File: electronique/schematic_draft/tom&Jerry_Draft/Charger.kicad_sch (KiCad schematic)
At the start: 56 parts, among them J201 Conn_01x02, J201 USB_C_Receptacle_USB2.0_16P, J202 Conn_01x02, J203 Conn_01x02, Q201 PMOS, U201 MP1475DJ-LF-P, U202 BQ25172DSGR

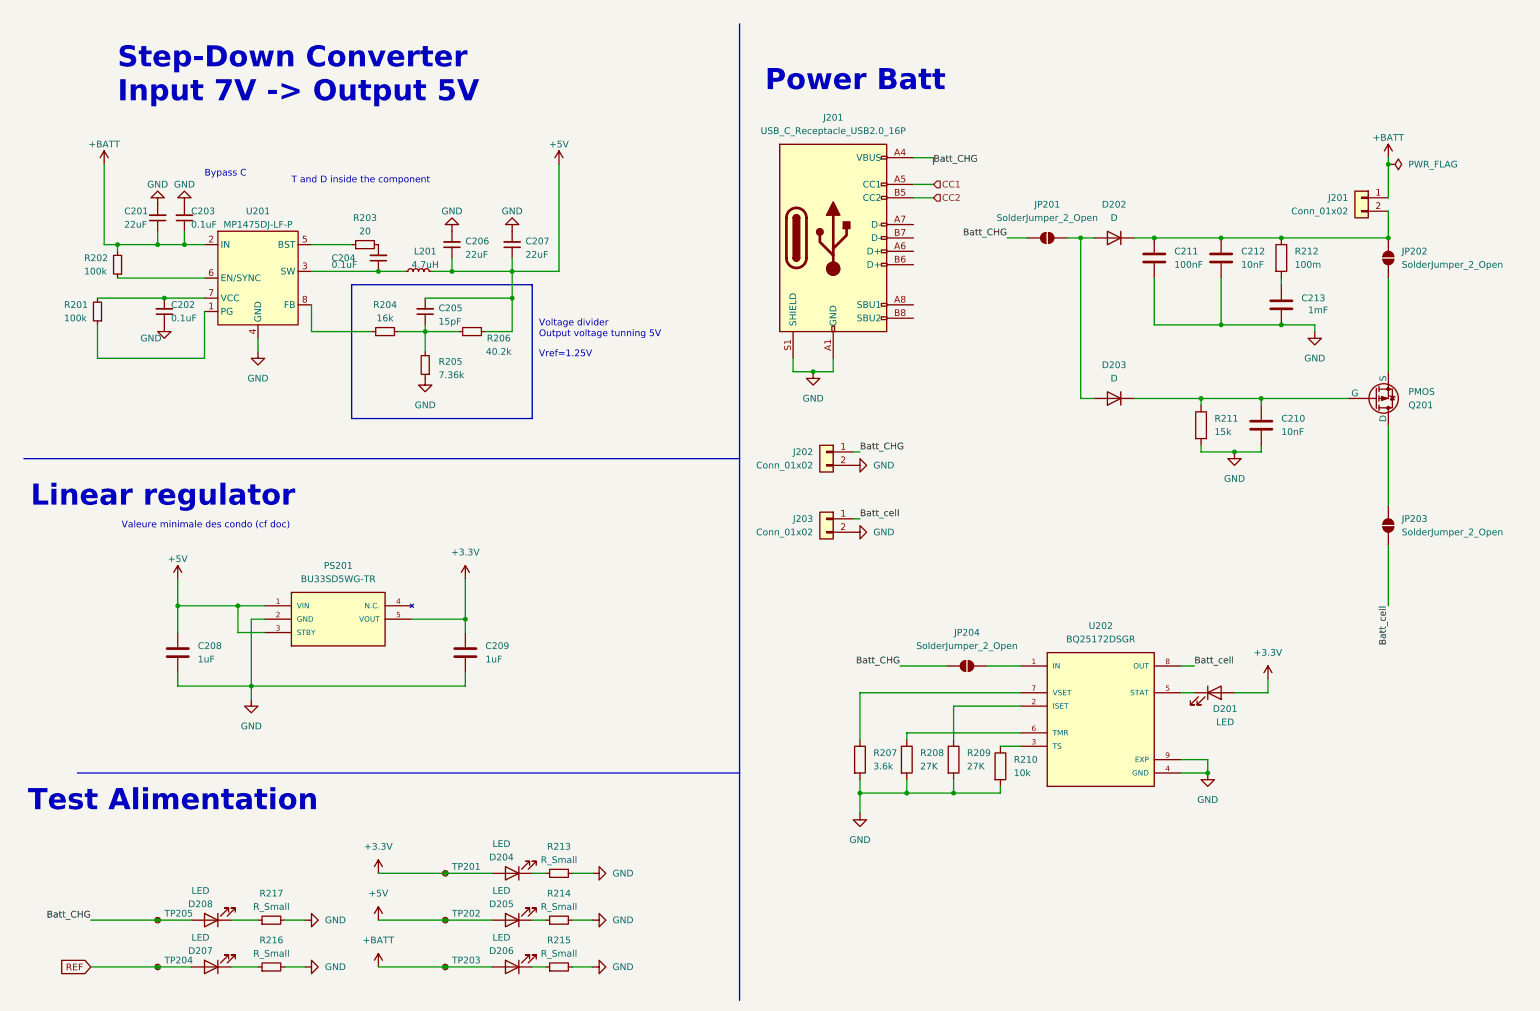
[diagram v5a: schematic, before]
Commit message: STM32 KiCAD v2.0 x CubeIDE - Pin definitif + schematic reviewed
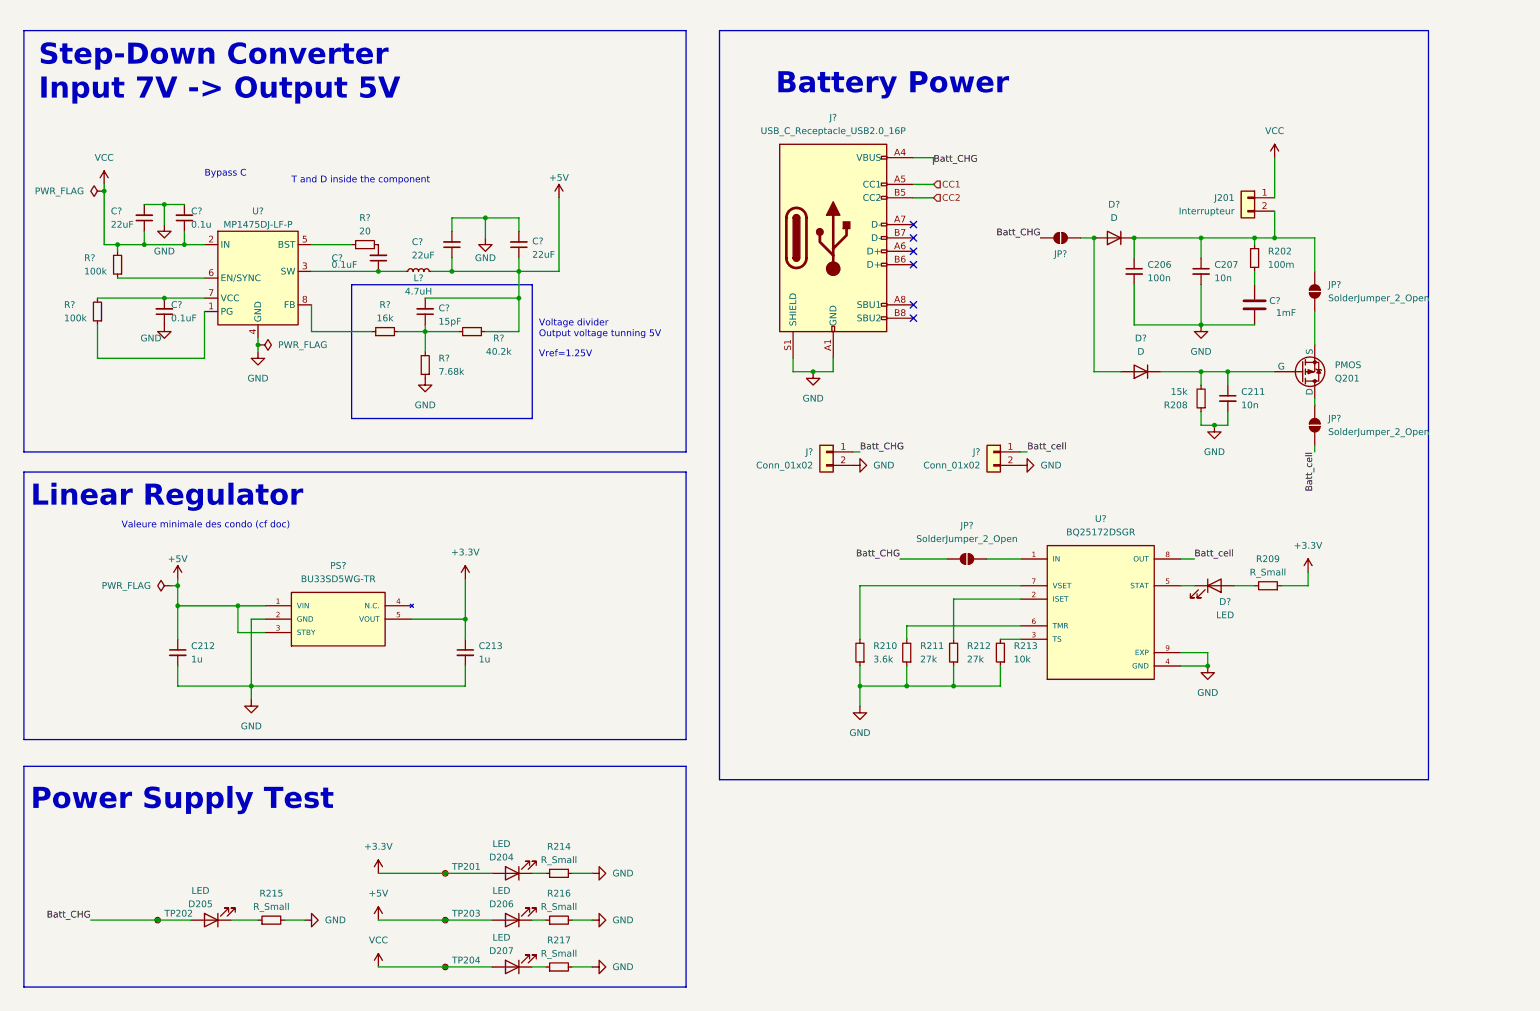
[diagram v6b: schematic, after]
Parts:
- removed C208, C209: 1uF, symbol Device:C
- removed C210, C212: 10nF, symbol Device:C
- removed C211: 100nF, symbol Device:C
- removed D207: LED, symbol Device:LED
- removed R207: 3.6k, symbol Device:R
- removed R208, R209: 27K, symbol Device:R
- removed R210: 10k, symbol Device:R
- removed R211: 15k, symbol Device:R
- removed R212: 100m, symbol Device:R
- removed R216: R_Small, symbol Device:R_Small
- removed TP204: TestPoint_Small, symbol Connector:TestPoint_Small
- added C206: 100n, symbol Device:C_Small
- added C207, C211: 10n, symbol Device:C_Small
- added C212, C213: 1u, symbol Device:C_Small
- added R202: 100m, symbol Device:R_Small
- added R208: 15k, symbol Device:R_Small
- added R209: R_Small, symbol Device:R_Small
- added R210: 3.6k, symbol Device:R_Small
- added R211, R212: 27k, symbol Device:R_Small
- added R213: 10k, symbol Device:R_Small
- C?: renamed from C203; value 0.1uF -> 0.1u
- J201: value Conn_01x02 -> Interrupteur
- R?: renamed from R205; value 7.36k -> 7.68k
- renumbered C213 to C?, C201 to C?, C202 to C?, C207 to C?, C206 to C?, C204 to C?, C205 to C?, D208 to D205, D205 to D206, D206 to D207, D203 to D?, D202 to D?, D201 to D?, J202 to J?, J203 to J?, J201 to J?, JP202 to JP?, JP204 to JP?, JP201 to JP?, JP203 to JP?, L201 to L?, PS201 to PS?, R213 to R214, R217 to R215, R214 to R216, R215 to R217, R206 to R?, R201 to R?, R204 to R?, R203 to R?, R202 to R?, TP205 to TP202, TP202 to TP203, TP203 to TP204, U202 to U?, U201 to U?
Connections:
- net +3.3V: now also C213.1, R209.1; no longer D?.2 (A)
- net +5V: now also L?.1, C212.1; no longer L?.2
- net GND: now also C206.2, C207.2, C211.2, C212.2, C213.2, R208.1, R210.1, R211.1, R212.1, R213.1
- net at D?.1 (K), Q201.2 (G): now also C211.1, R208.2
- net at C?.1: now also R202.2
- net at D?.1 (K), J201.2 (Pin_2), JP?.2 (B): now also C206.1, C207.1, R202.1
- net at C?.1, U?.3 (SW): now also L?.2; no longer L?.1
- net at U?.6 (TMR): now also R211.2
- net at U?.2 (ISET): now also R212.2
- net at U?.3 (TS): now also R213.2
- net at U?.7 (VSET): now also R210.2
- net +BATT renamed VCC
- new net: D?.2 (A), R209.2
- no-connect marks 0 -> 6
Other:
- note added: "Battery Power"
- note added: "Linear Regulator"
- note added: "Power Supply Test"
- note removed: "Linear regulator"
- note removed: "Power Batt"
- note removed: "Test Alimentation"
- moved on the sheet: C?, D?, J201, J?, JP?, L?, Q201, U?

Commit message: Adding footprint V0.1
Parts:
- C206, C207, C211: footprint (none) -> Capacitor_SMD:C_0402_1005Metric
- C212, C213: footprint (none) -> Capacitor_SMD:C_0603_1608Metric
- C? (x4): footprint Capacitor_SMD:C_0603_1608Metric_Pad1.08x0.95mm_HandSolder -> Capacitor_SMD:C_0402_1005Metric
- C?: footprint (none) -> Tom&Jerry:PQFN80P300X500X100-14N
- C? (x3): footprint Capacitor_SMD:C_0603_1608Metric_Pad1.08x0.95mm_HandSolder -> Capacitor_SMD:C_0805_2012Metric
- D204, D205, D206, D207, D?: footprint (none) -> LED_SMD:LED_0603_1608Metric_Pad1.05x0.95mm_HandSolder
- J201: footprint (none) -> Tom&Jerry:Switch-3
- J? (x2): footprint (none) -> Connector_JST:JST_XH_S2B-XH-A-1_1x02_P2.50mm_Horizontal
- J?: footprint (none) -> Connector_USB:USB_C_Receptacle_HRO_TYPE-C-31-M-12
- JP? (x4): footprint (none) -> Jumper:SolderJumper-2_P1.3mm_Open_TrianglePad1.0x1.5mm
- L?: footprint Library:INDPM4141X210N -> Inductor_SMD:L_0603_1608Metric_Pad1.05x0.95mm_HandSolder
- PS?: footprint BU33SD5WG-TR:SOT95P280X125-5N -> Tom&Jerry:SOT95P280X125-5N
- R202, R208, R209, R210, R211, R212, R213: footprint (none) -> Resistor_SMD:R_0402_1005Metric
- R214, R215, R216, R217: value R_Small -> 3.3k; footprint (none) -> Resistor_SMD:R_0402_1005Metric
- R? (x5): footprint Resistor_SMD:R_0603_1608Metric_Pad0.98x0.95mm_HandSolder -> Resistor_SMD:R_0402_1005Metric
- R?: footprint Resistor_SMD:R_0805_2012Metric_Pad1.20x1.40mm_HandSolder -> Resistor_SMD:R_0402_1005Metric
- TP201, TP202, TP203, TP204: footprint (none) -> Test_Point:TestPoint_Pad_D1.5mm
- U?: footprint BQ25172DSGR:IC_BQ25172DSGR -> Tom&Jerry:IC_BQ25172DSGR
- U?: footprint Library:SOT65P280X100-8N -> Tom&Jerry:SOT65P280X100-8N
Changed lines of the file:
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@@
 			)
 		)
-		(property "Footprint" "Capacitor_SMD:C_0603_1608Metric_Pad1.08x0.95mm_HandSolder"
+		(property "Footprint" "Capacitor_SMD:C_0402_1005Metric"
 			(at 45.72 50.8 0)
 			(effects
@@
 			)
 		)
-		(property "Footprint" ""
+		(property "Footprint" "Capacitor_SMD:C_0603_1608Metric"
 			(at 44.45 133.35 0)
 			(effects
@@
 			)
 		)
-		(property "Footprint" ""
+		(property "Footprint" "Tom&Jerry:PQFN80P300X500X100-14N"
 			(at 249.8852 71.12 0)
 			(effects
@@
 			)
 		)
-		(property "Value" "R_Small"
+		(property "Value" "3.3k"
 			(at 116.84 190.5 90)
 			(effects
@@
 			)
 		)
-		(property "Footprint" ""
+		(property "Footprint" "Resistor_SMD:R_0402_1005Metric"
 			(at 116.84 193.04 0)
 			(effects
@@
 			)
 		)
-		(property "Footprint" ""
+		(property "Footprint" "Tom&Jerry:Switch-3"
 			(at 247.65 46.99 0)
 			(effects
@@
 			)
 		)
-		(property "Value" "R_Small"
+		(property "Value" "3.3k"
 			(at 116.84 172.72 90)
 			(effects
@@
 			)
 		)
-		(property "Footprint" ""
+		(property "Footprint" "Resistor_SMD:R_0402_1005Metric"
 			(at 116.84 175.26 0)
 			(effects
@@
 			)
 		)
-		(property "Footprint" "Library:INDPM4141X210N"
+		(property "Footprint" "Inductor_SMD:L_0603_1608Metric_Pad1.05x0.95mm_HandSolder"
 			(at 90.17 60.96 0)
 			(effects
@@
 			)
 		)
-		(property "Footprint" "Resistor_SMD:R_0603_1608Metric_Pad0.98x0.95mm_HandSolder"
+		(property "Footprint" "Resistor_SMD:R_0402_1005Metric"
 			(at 100.33 72.39 0)
 			(effects
@@
 			)
 		)
-		(property "Footprint" "BQ25172DSGR:IC_BQ25172DSGR"
+		(property "Footprint" "Tom&Jerry:IC_BQ25172DSGR"
 			(at 219.71 125.73 0)
 			(effects
@@
 			)
 		)
-		(property "Footprint" "Capacitor_SMD:C_0603_1608Metric_Pad1.08x0.95mm_HandSolder"
+		(property "Footprint" "Capacitor_SMD:C_0805_2012Metric"
 			(at 38.1 50.8 0)
 			(effects
@@
 			)
 		)
-		(property "Footprint" "BU33SD5WG-TR:SOT95P280X125-5N"
+		(property "Footprint" "Tom&Jerry:SOT95P280X125-5N"
 			(at 60.96 114.3 0)
 			(effects
@@
 			)
 		)
-		(property "Footprint" "Resistor_SMD:R_0603_1608Metric_Pad0.98x0.95mm_HandSolder"
+		(property "Footprint" "Resistor_SMD:R_0402_1005Metric"
 			(at 91.44 78.74 0)
 			(effects
@@
 			)
 		)
-		(property "Footprint" ""
+		(property "Footprint" "Jumper:SolderJumper-2_P1.3mm_Open_TrianglePad1.0x1.5mm"
 			(at 260.35 64.77 0)
 			(effects
@@
 			)
 		)
-		(property "Footprint" "Resistor_SMD:R_0603_1608Metric_Pad0.98x0.95mm_HandSolder"
+		(property "Footprint" "Resistor_SMD:R_0402_1005Metric"
 			(at 29.21 68.58 0)
 			(effects
@@
 			)
 		)
-		(property "Footprint" ""
+		(property "Footprint" "Capacitor_SMD:C_0402_1005Metric"
 			(at 238.76 60.96 0)
 			(effects
@@
 			)
 		)
-		(property "Footprint" ""
+		(property "Footprint" "Resistor_SMD:R_0402_1005Metric"
 			(at 173.99 133.35 0)
 			(effects
@@
 			)
 		)
-		(property "Footprint" ""
+		(property "Footprint" "LED_SMD:LED_0603_1608Metric_Pad1.05x0.95mm_HandSolder"
 			(at 50.8 184.15 0)
 			(effects
@@
 			)
 		)
-		(property "Footprint" ""
+		(property "Footprint" "Connector_JST:JST_XH_S2B-XH-A-1_1x02_P2.50mm_Horizontal"
 			(at 167.64 95.25 0)
 			(effects
@@
 			)
 		)
-		(property "Footprint" ""
+		(property "Footprint" "Test_Point:TestPoint_Pad_D1.5mm"
 			(at 100.33 175.26 0)
 			(effects
@@
 			)
 		)
-		(property "Footprint" "Resistor_SMD:R_0603_1608Metric_Pad0.98x0.95mm_HandSolder"
+		(property "Footprint" "Resistor_SMD:R_0402_1005Metric"
 			(at 83.82 72.39 0)
 			(effects
@@
 			)
 		)
-		(property "Footprint" ""
+		(property "Footprint" "Connector_JST:JST_XH_S2B-XH-A-1_1x02_P2.50mm_Horizontal"
 			(at 199.39 95.25 0)
 			(effects
@@
 			)
 		)
-		(property "Footprint" ""
+		(property "Footprint" "LED_SMD:LED_0603_1608Metric_Pad1.05x0.95mm_HandSolder"
 			(at 107.95 175.26 0)
 			(effects
@@
 			)
 		)
-		(property "Footprint" ""
+		(property "Footprint" "Resistor_SMD:R_0402_1005Metric"
 			(at 191.77 133.35 0)
 			(effects
@@
 			)
 		)
-		(property "Value" "R_Small"
+		(property "Value" "3.3k"
 			(at 116.84 181.61 90)
 			(effects
@@
 			)
 		)
-		(property "Footprint" ""
+		(property "Footprint" "Resistor_SMD:R_0402_1005Metric"
 			(at 116.84 184.15 0)
 			(effects
@@
 			)
 		)
-		(property "Footprint" ""
+		(property "Footprint" "Connector_USB:USB_C_Receptacle_HRO_TYPE-C-31-M-12"
 			(at 172.72 54.61 0)
 			(effects
@@
 			)
 		)
-		(property "Footprint" ""
+		(property "Footprint" "Test_Point:TestPoint_Pad_D1.5mm"
 			(at 100.33 193.04 0)
 			(effects
@@
 			)
 		)
-		(property "Footprint" ""
+		(property "Footprint" "Capacitor_SMD:C_0402_1005Metric"
 			(at 243.84 85.09 0)
 			(effects
@@
 			)
 		)
-		(property "Footprint" ""
+		(property "Footprint" "Test_Point:TestPoint_Pad_D1.5mm"
 			(at 100.33 184.15 0)
 			(effects
@@
 			)
 		)
-		(property "Footprint" ""
+		(property "Footprint" "Capacitor_SMD:C_0603_1608Metric"
 			(at 99.06 133.35 0)
 			(effects
@@
 			)
 		)
-		(property "Footprint" "Capacitor_SMD:C_0603_1608Metric_Pad1.08x0.95mm_HandSolder"
+		(property "Footprint" "Capacitor_SMD:C_0402_1005Metric"
 			(at 41.91 68.58 0)
 			(effects
@@
 			)
 		)
-		(property "Footprint" "Capacitor_SMD:C_0603_1608Metric_Pad1.08x0.95mm_HandSolder"
+		(property "Footprint" "Capacitor_SMD:C_0805_2012Metric"
 			(at 109.22 55.88 0)
 			(effects
@@
 			)
 		)
-		(property "Footprint" ""
+		(property "Footprint" "Resistor_SMD:R_0402_1005Metric"
 			(at 251.46 120.65 0)
 			(effects
@@
 			)
 		)
-		(property "Footprint" "Resistor_SMD:R_0805_2012Metric_Pad1.20x1.40mm_HandSolder"
+		(property "Footprint" "Resistor_SMD:R_0402_1005Metric"
 			(at 80.01 55.88 0)
 			(effects
@@
 			)
 		)
-		(property "Footprint" "Resistor_SMD:R_0603_1608Metric_Pad0.98x0.95mm_HandSolder"
+		(property "Footprint" "Resistor_SMD:R_0402_1005Metric"
 			(at 33.02 59.69 0)
 			(effects
@@
 			)
 		)
-		(property "Footprint" ""
+		(property "Footprint" "Resistor_SMD:R_0402_1005Metric"
 			(at 238.76 85.09 0)
 			(effects
@@
 			)
 		)
-		(property "Footprint" ""
+		(property "Footprint" "Jumper:SolderJumper-2_P1.3mm_Open_TrianglePad1.0x1.5mm"
 			(at 194.31 115.57 0)
 			(effects
@@
 			)
 		)
-		(property "Footprint" "Library:SOT65P280X100-8N"
+		(property "Footprint" "Tom&Jerry:SOT65P280X100-8N"
 			(at 53.34 53.34 0)
 			(effects
@@
 			)
 		)
-		(property "Footprint" ""
+		(property "Footprint" "LED_SMD:LED_0603_1608Metric_Pad1.05x0.95mm_HandSolder"
 			(at 107.95 193.04 0)
 			(effects
@@
 			)
 		)
-		(property "Footprint" "Capacitor_SMD:C_0603_1608Metric_Pad1.08x0.95mm_HandSolder"
+		(property "Footprint" "Capacitor_SMD:C_0805_2012Metric"
 			(at 96.52 55.88 0)
 			(effects
@@
 			)
 		)
-		(property "Footprint" ""
+		(property "Footprint" "Resistor_SMD:R_0402_1005Metric"
 			(at 182.88 133.35 0)
 			(effects
@@
 			)
 		)
-		(property "Footprint" ""
+		(property "Footprint" "Jumper:SolderJumper-2_P1.3mm_Open_TrianglePad1.0x1.5mm"
 			(at 212.09 54.61 0)
 			(effects
@@
 			)
 		)
-		(property "Footprint" ""
+		(property "Footprint" "LED_SMD:LED_0603_1608Metric_Pad1.05x0.95mm_HandSolder"
 			(at 241.3 120.65 0)
 			(effects
@@
 			)
 		)
-		(property "Footprint" ""
+		(property "Footprint" "Test_Point:TestPoint_Pad_D1.5mm"
 			(at 45.72 184.15 0)
 			(effects
@@
 			)
 		)
-		(property "Footprint" "Capacitor_SMD:C_0603_1608Metric_Pad1.08x0.95mm_HandSolder"
+		(property "Footprint" "Capacitor_SMD:C_0402_1005Metric"
 			(at 82.55 58.42 0)
 			(effects
@@
 			)
 		)
-		(property "Footprint" "Capacitor_SMD:C_0603_1608Metric_Pad1.08x0.95mm_HandSolder"
+		(property "Footprint" "Capacitor_SMD:C_0402_1005Metric"
 			(at 91.44 68.58 0)
 			(effects
@@
 			)
 		)
-		(property "Footprint" ""
+		(property "Footprint" "Capacitor_SMD:C_0402_1005Metric"
 			(at 226.06 60.96 0)
 			(effects
@@
 			)
 		)
-		(property "Footprint" ""
+		(property "Footprint" "LED_SMD:LED_0603_1608Metric_Pad1.05x0.95mm_HandSolder"
 			(at 107.95 184.15 0)
 			(effects
@@
 			)
 		)
-		(property "Footprint" ""
+		(property "Footprint" "Resistor_SMD:R_0402_1005Metric"
 			(at 200.66 133.35 0)
 			(effects
@@
 			)
 		)
-		(property "Footprint" ""
+		(property "Footprint" "Resistor_SMD:R_0402_1005Metric"
 			(at 248.92 58.42 0)
 			(effects
@@
 			)
 		)
-		(property "Value" "R_Small"
+		(property "Value" "3.3k"
 			(at 62.23 181.61 90)
 			(effects
@@
 			)
 		)
-		(property "Footprint" ""
+		(property "Footprint" "Resistor_SMD:R_0402_1005Metric"
 			(at 62.23 184.15 0)
 			(effects
@@
 			)
 		)
-		(property "Footprint" ""
+		(property "Footprint" "Jumper:SolderJumper-2_P1.3mm_Open_TrianglePad1.0x1.5mm"
 			(at 260.35 90.17 0)
 			(effects

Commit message: Changing footprint V0.2
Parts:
- C?: footprint Tom&Jerry:PQFN80P300X500X100-14N -> Tom&Jerry:CAPAE1350X1400N
- D? (x2): footprint (none) -> Tom&Jerry:SODFL4825X110N
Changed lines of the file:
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@@
 			)
 		)
-		(property "Footprint" "Tom&Jerry:PQFN80P300X500X100-14N"
+		(property "Footprint" "Tom&Jerry:CAPAE1350X1400N"
 			(at 249.8852 71.12 0)
 			(effects
@@
 			)
 		)
-		(property "Footprint" ""
+		(property "Footprint" "Tom&Jerry:SODFL4825X110N"
 			(at 227.33 80.01 0)
 			(effects
@@
 			)
 		)
-		(property "Footprint" ""
+		(property "Footprint" "Tom&Jerry:SODFL4825X110N"
 			(at 222.25 54.61 0)
 			(effects
